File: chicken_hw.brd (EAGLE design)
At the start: 25.7 x 38.1 mm, 19 parts

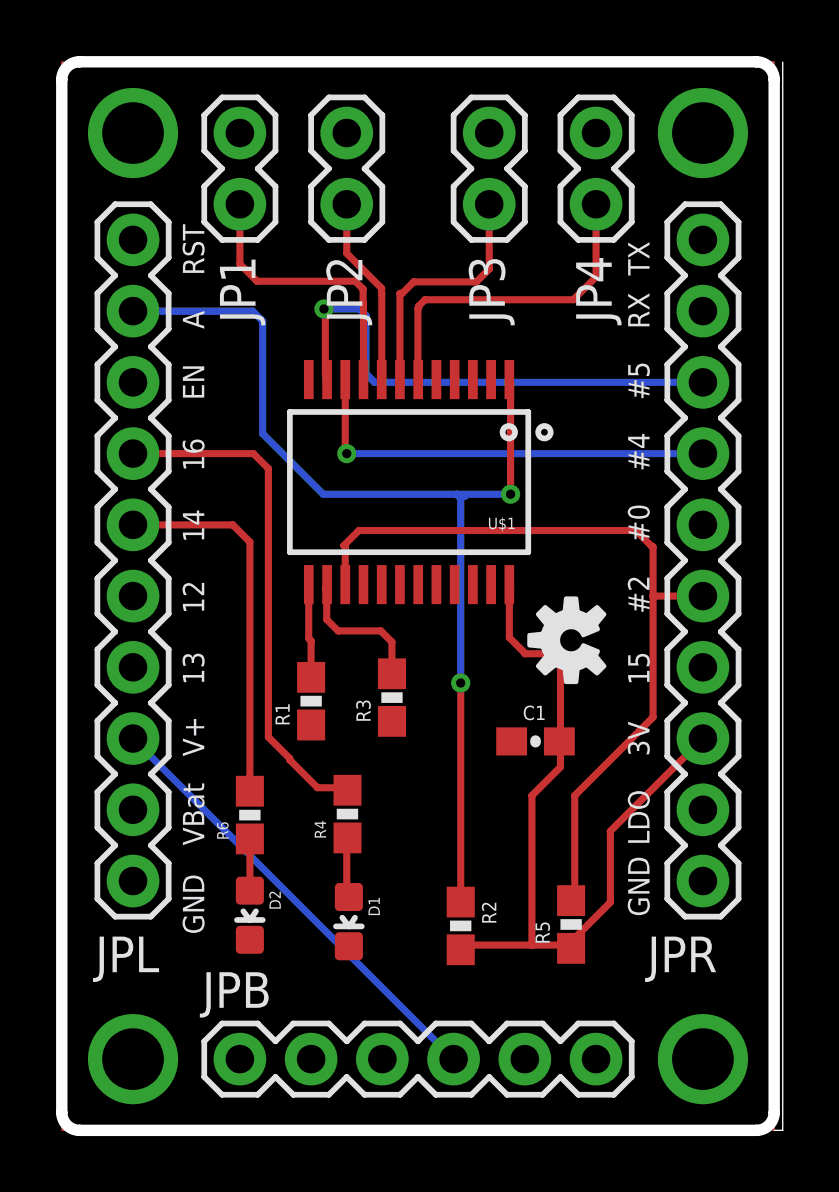
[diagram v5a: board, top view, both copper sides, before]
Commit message: Enable ESP8266 deepsleep by connecting GPIO16 to RESET - bump to ver 0.2
Remove led's on GPIO 16,14 and move them to GPIO 12, 13
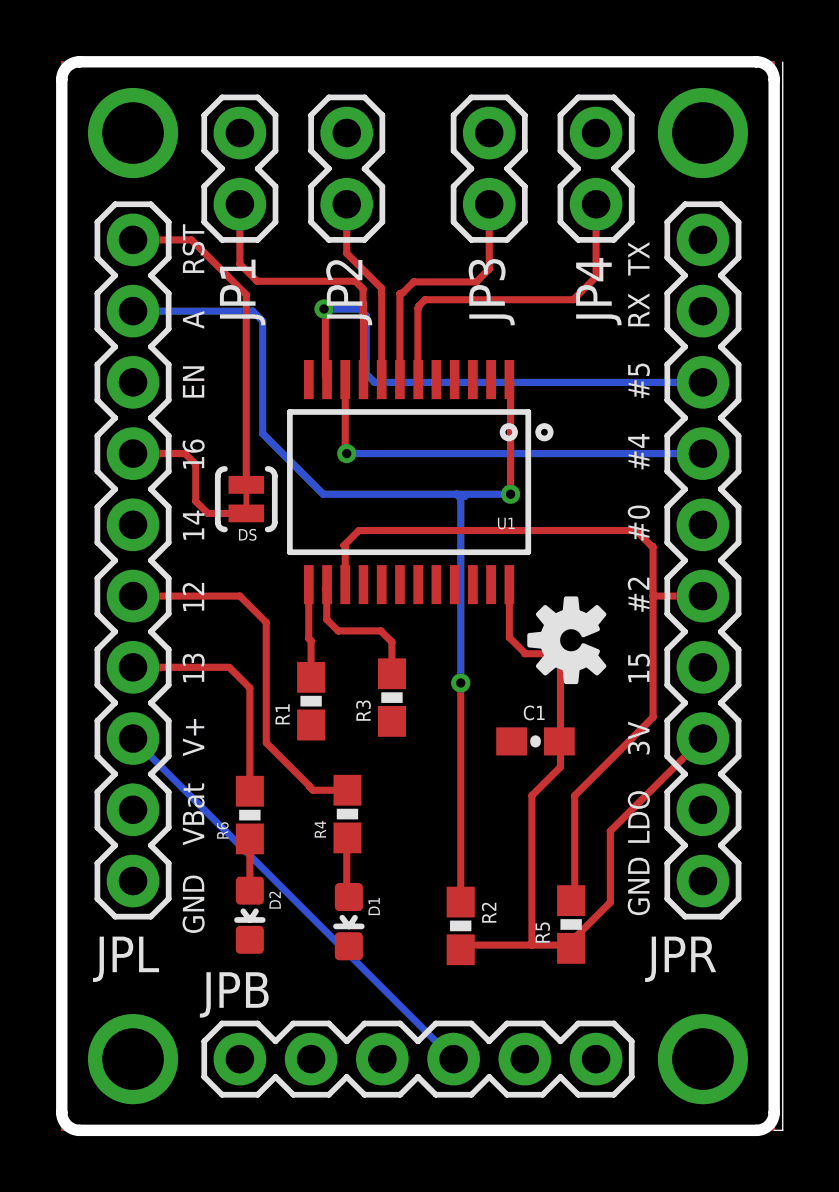
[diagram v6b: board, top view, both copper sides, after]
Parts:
- added DS: JUMPER-PAD-2-NC_BY_TRACE, SparkFun-Passives:PAD-JUMPER-2-NC_BY_TRACE_YES_SILK
- renumbered U$1 to U1
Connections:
- net GPIO12: now also R4.2
- net GPIO13: now also R6.2
- net GPIO14: no longer R6.2
- net GPIO16: now also DS.1; no longer R4.2
- net RST: now also DS.2
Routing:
- net GPIO14: track 13.3 -> 0.00 mm
- net GPIO12: track 0.00 -> 13.0 mm
- net GPIO16: track 18.3 -> 5.70 mm
- net RST: track 0.00 -> 11.6 mm
- net GPIO13: track 0.00 -> 8.15 mm
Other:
- board text added: "4-input Temp Sensor jason.k.holden@gmail.com ver 0.2 11-15-2015"
- board text removed: "4-input Temp Sensor jason.k.holden@gmail.com ver 0.1 11-8-2015"
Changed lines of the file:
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@@
 <text x="12.6492" y="19.1516" size="1.016" layer="22" font="vector" ratio="12" rot="MR90" align="center">4-input Temp Sensor
 jason.k.holden@gmail.com
-ver 0.1 11-8-2015</text>
+ver 0.2 11-15-2015</text>
 </plain>
 <attributes>
@@
 <attribute name="VALUE" x="19.685" y="33.02" size="1.27" layer="27" rot="R270"/>
 </element>
-<element name="U$1" library="SparkFun-AnalogIC" package="SSOP24" value="MUX-74HC4067SMD" x="12.3825" y="23.114" rot="R180">
+<element name="U1" library="SparkFun-AnalogIC" package="SSOP24" value="MUX-74HC4067SMD" x="12.3825" y="23.114" smashed="yes" rot="R180">
 <attribute name="PROD_ID" value="IC-08252" x="12.3825" y="23.114" size="1.778" layer="27" rot="R180" display="off"/>
+<attribute name="NAME" x="16.1925" y="21.844" size="0.4064" layer="25" font="vector" ratio="12" rot="R180"/>
+<attribute name="VALUE" x="15.1765" y="23.368" size="0.4064" layer="27" font="vector" ratio="12" rot="R180"/>
 </element>
 <element name="JP1" library="SparkFun-Connectors" package="1X02" value="" x="6.35" y="35.56" smashed="yes" rot="R270">
@@
 <element name="FRAME1" library="SparkFun-Aesthetics" package="CREATIVE_COMMONS" value="FRAME-LETTER" x="-3.937" y="-9.6012" smashed="yes"/>
 <element name="LOGO1" library="SparkFun-Aesthetics" package="OSHW-LOGO-S" value="OSHW-LOGOS" x="18.161" y="17.4752" rot="R90"/>
+<element name="DS" library="SparkFun-Passives" package="PAD-JUMPER-2-NC_BY_TRACE_YES_SILK" value="JUMPER-PAD-2-NC_BY_TRACE" x="6.5786" y="22.5044" smashed="yes" rot="R90">
+<attribute name="NAME" x="6.9723" y="21.4376" size="0.4064" layer="25" font="vector" ratio="12" rot="R180"/>
+</element>
 </elements>
 <signals>
 <signal name="RST">
 <contactref element="JPL" pad="1"/>
+<contactref element="DS" pad="2"/>
+<wire x1="6.5786" y1="23.0124" x2="6.5786" y2="29.7942" width="0.254" layer="1"/>
+<wire x1="6.5786" y1="29.7942" x2="4.6228" y2="31.75" width="0.254" layer="1"/>
+<wire x1="2.54" y1="31.75" x2="4.6228" y2="31.75" width="0.254" layer="1"/>
 </signal>
 <signal name="A">
 <contactref element="JPL" pad="2"/>
-<contactref element="U$1" pad="1"/>
+<contactref element="U1" pad="1"/>
 <contactref element="R2" pad="1"/>
 <via x="14.224" y="15.9512" extent="1-16" drill="0.3302"/>
@@
 <contactref element="JPL" pad="3"/>
 </signal>
-<signal name="GPIO16">
-<contactref element="JPL" pad="4"/>
-<contactref element="R4" pad="2"/>
-<wire x1="8.128" y1="13.208" x2="8.128" y2="13.2588" width="0.254" layer="1"/>
-<wire x1="8.128" y1="13.2588" x2="7.366" y2="14.0208" width="0.254" layer="1"/>
-<wire x1="7.366" y1="14.0208" x2="7.366" y2="23.5966" width="0.254" layer="1"/>
-<wire x1="2.54" y1="24.13" x2="6.8326" y2="24.13" width="0.254" layer="1"/>
-<wire x1="6.8326" y1="24.13" x2="7.366" y2="23.5966" width="0.254" layer="1"/>
-<wire x1="10.1854" y1="12.1276" x2="10.1854" y2="12.192" width="0.254" layer="1"/>
-<wire x1="10.1854" y1="12.192" x2="10.2108" y2="12.2174" width="0.254" layer="1"/>
-<wire x1="10.2108" y1="12.2174" x2="9.1186" y2="12.2174" width="0.254" layer="1"/>
-<wire x1="9.1186" y1="12.2174" x2="8.128" y2="13.208" width="0.254" layer="1"/>
-</signal>
-<signal name="GPIO14">
-<contactref element="JPL" pad="5"/>
-<contactref element="R6" pad="2"/>
-<wire x1="2.54" y1="21.59" x2="6.096" y2="21.59" width="0.254" layer="1"/>
-<wire x1="6.096" y1="21.59" x2="6.7056" y2="20.9804" width="0.254" layer="1"/>
-<wire x1="6.7056" y1="12.0895" x2="6.7056" y2="20.9804" width="0.254" layer="1"/>
-</signal>
 <signal name="GPIO12">
 <contactref element="JPL" pad="6"/>
+<contactref element="R4" pad="2"/>
+<wire x1="10.1854" y1="12.1276" x2="8.9544" y2="12.1276" width="0.254" layer="1"/>
+<wire x1="8.9544" y1="12.1276" x2="8.8392" y2="12.2428" width="0.254" layer="1"/>
+<wire x1="8.8392" y1="12.2428" x2="8.8392" y2="12.2682" width="0.254" layer="1"/>
+<wire x1="8.8392" y1="12.2682" x2="7.2898" y2="13.8176" width="0.254" layer="1"/>
+<wire x1="7.2898" y1="13.8176" x2="7.2898" y2="18.1102" width="0.254" layer="1"/>
+<wire x1="2.54" y1="19.05" x2="6.35" y2="19.05" width="0.254" layer="1"/>
+<wire x1="6.35" y1="19.05" x2="7.2898" y2="18.1102" width="0.254" layer="1"/>
 </signal>
 <signal name="GPIO13">
 <contactref element="JPL" pad="7"/>
+<contactref element="R6" pad="2"/>
+<wire x1="6.7056" y1="12.0895" x2="6.7056" y2="15.7734" width="0.254" layer="1"/>
+<wire x1="6.7056" y1="15.7734" x2="5.969" y2="16.51" width="0.254" layer="1"/>
+<wire x1="2.54" y1="16.51" x2="5.969" y2="16.51" width="0.254" layer="1"/>
 </signal>
 <signal name="VPLUS">
@@
 <signal name="GPIO4">
 <contactref element="JPR" pad="4"/>
-<contactref element="U$1" pad="10"/>
+<contactref element="U1" pad="10"/>
 <wire x1="22.86" y1="24.13" x2="10.16" y2="24.13" width="0.254" layer="16"/>
 <via x="10.16" y="24.13" extent="1-16" drill="0.3302"/>
@@
 <signal name="GPIO5">
 <contactref element="JPR" pad="3"/>
-<contactref element="U$1" pad="11"/>
+<contactref element="U1" pad="11"/>
 <wire x1="22.86" y1="26.67" x2="11.1506" y2="26.67" width="0.254" layer="16"/>
 <wire x1="9.398" y1="26.924" x2="9.4575" y2="26.77" width="0.254" layer="1"/>
@@
 <contactref element="JPB" pad="6"/>
 <contactref element="JPL" pad="10"/>
-<contactref element="U$1" pad="12"/>
+<contactref element="U1" pad="12"/>
 <contactref element="JP1" pad="1"/>
 <contactref element="JP2" pad="1"/>
@@
 <signal name="3.3V">
 <contactref element="JPR" pad="8"/>
-<contactref element="U$1" pad="24"/>
+<contactref element="U1" pad="24"/>
 <contactref element="C1" pad="1"/>
 <contactref element="R5" pad="2"/>
@@
 </signal>
 <signal name="EN_MUX">
-<contactref element="U$1" pad="15"/>
+<contactref element="U1" pad="15"/>
 <contactref element="JPR" pad="6"/>
 <contactref element="R5" pad="1"/>
@@
 <signal name="N$2">
 <contactref element="JP1" pad="2"/>
-<contactref element="U$1" pad="9"/>
+<contactref element="U1" pad="9"/>
 <wire x1="10.7575" y1="26.77" x2="10.7575" y2="29.4773" width="0.254" layer="1"/>
 <wire x1="10.4648" y1="30.2768" x2="6.9596" y2="30.2768" width="0.254" layer="1"/>
@@
 <signal name="N$3">
 <contactref element="JP2" pad="2"/>
-<contactref element="U$1" pad="8"/>
+<contactref element="U1" pad="8"/>
 <wire x1="11.4075" y1="26.77" x2="11.4075" y2="29.8167" width="0.254" layer="1"/>
 <wire x1="11.4075" y1="29.8167" x2="11.4046" y2="29.8196" width="0.254" layer="1"/>
@@
 <signal name="N$4">
 <contactref element="JP3" pad="2"/>
-<contactref element="U$1" pad="7"/>
+<contactref element="U1" pad="7"/>
 <wire x1="15.24" y1="33.02" x2="15.24" y2="30.7086" width="0.254" layer="1"/>
 <wire x1="15.24" y1="30.7086" x2="14.7828" y2="30.2514" width="0.254" layer="1"/>
@@
 <signal name="N$5">
 <contactref element="JP4" pad="2"/>
-<contactref element="U$1" pad="6"/>
+<contactref element="U1" pad="6"/>
 <wire x1="12.7" y1="26.924" x2="12.7" y2="29.3116" width="0.254" layer="1"/>
 <wire x1="12.7" y1="29.3116" x2="12.7254" y2="29.337" width="0.254" layer="1"/>
@@
 </signal>
 <signal name="N$1">
-<contactref element="U$1" pad="13"/>
+<contactref element="U1" pad="13"/>
 <contactref element="R1" pad="2"/>
 <wire x1="8.89" y1="16.1535" x2="8.89" y2="17.4498" width="0.254" layer="1"/>
@@
 </signal>
 <signal name="N$6">
-<contactref element="U$1" pad="14"/>
+<contactref element="U1" pad="14"/>
 <contactref element="R3" pad="2"/>
 <wire x1="9.398" y1="19.304" x2="9.4575" y2="19.458" width="0.254" layer="1"/>
@@
 <wire x1="6.7056" y1="10.3895" x2="6.7056" y2="8.5478" width="0.254" layer="1"/>
 </signal>
+<signal name="GPIO14">
+<contactref element="JPL" pad="5"/>
+</signal>
+<signal name="GPIO16">
+<contactref element="JPL" pad="4"/>
+<contactref element="DS" pad="1"/>
+<wire x1="2.54" y1="24.13" x2="4.3942" y2="24.13" width="0.254" layer="1"/>
+<wire x1="4.3942" y1="24.13" x2="4.7752" y2="23.749" width="0.254" layer="1"/>
+<wire x1="4.7752" y1="23.749" x2="4.7752" y2="22.4282" width="0.254" layer="1"/>
+<wire x1="4.7752" y1="22.4282" x2="5.207" y2="21.9964" width="0.254" layer="1"/>
+<wire x1="6.5786" y1="21.9964" x2="5.207" y2="21.9964" width="0.254" layer="1"/>
+</signal>
 </signals>

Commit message: Switch to 8to1 mux to save on cost
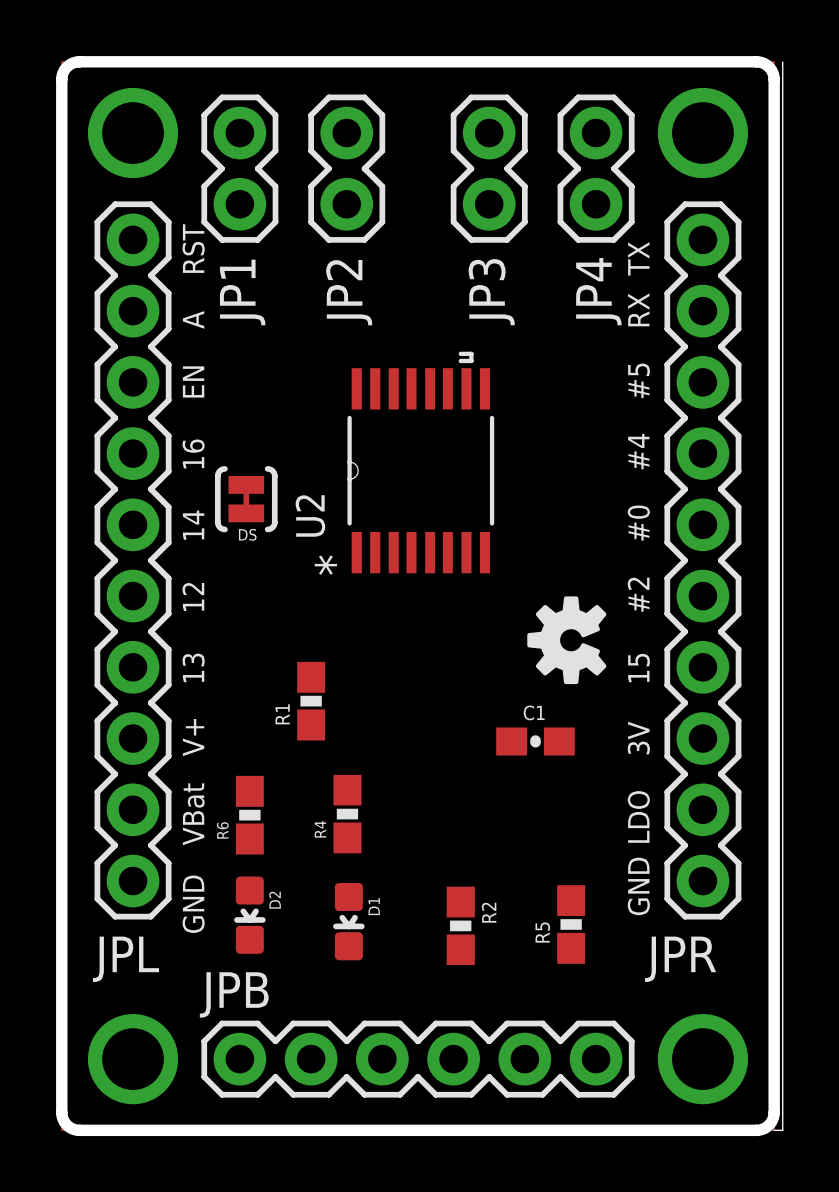
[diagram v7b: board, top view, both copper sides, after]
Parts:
- removed R3: 10k, SparkFun-Resistors:0603-RES
- removed U1: MUX-74HC4067SMD, SparkFun-AnalogIC:SSOP24
- added U2: CD74HC4051PWR, Texas Instruments_By_element14_Batch_1:SOP65P640X120-16N
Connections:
- removed net N$6: R3.2, U1.14
- new net VCC: U2.16
- net 3.3V: no longer U1.24
- net A: now also U2.3; no longer U1.1
- net EN_MUX: now also U2.6; no longer U1.15
- net GND: now also U2.7, U2.8; no longer R3.1, U1.12
- net GPIO4: now also U2.11; no longer U1.10
- net GPIO5: now also U2.10; no longer U1.11
- net N$1: no longer U1.13
- net N$2: now also U2.13; no longer U1.9
- net N$3: now also U2.14; no longer U1.8
- net N$4: now also U2.15; no longer U1.7
- net N$5: now also U2.12; no longer U1.6
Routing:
- net A: track 37.1 -> 0.00 mm, vias 2 -> 0
- net 3.3V: track 28.3 -> 0.00 mm
- net EN_MUX: track 28.3 -> 0.00 mm
- net GPIO5: track 18.4 -> 0.00 mm, vias 1 -> 0
- net VPLUS: track 16.2 -> 0.00 mm
- net GPIO4: track 15.4 -> 0.00 mm, vias 1 -> 0
- net GPIO12: track 13.0 -> 0.00 mm
- net N$5: track 11.8 -> 0.00 mm
- net RST: track 11.6 -> 0.00 mm
- net N$2: track 10.1 -> 0.00 mm
- net N$4: track 8.92 -> 0.00 mm
- net GPIO13: track 8.15 -> 0.00 mm
- net N$3: track 6.77 -> 0.00 mm
- net GPIO16: track 5.70 -> 0.00 mm
- net N$6: track 5.09 -> 0.00 mm
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
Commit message: Fully routed 8:1 mux, ready for production
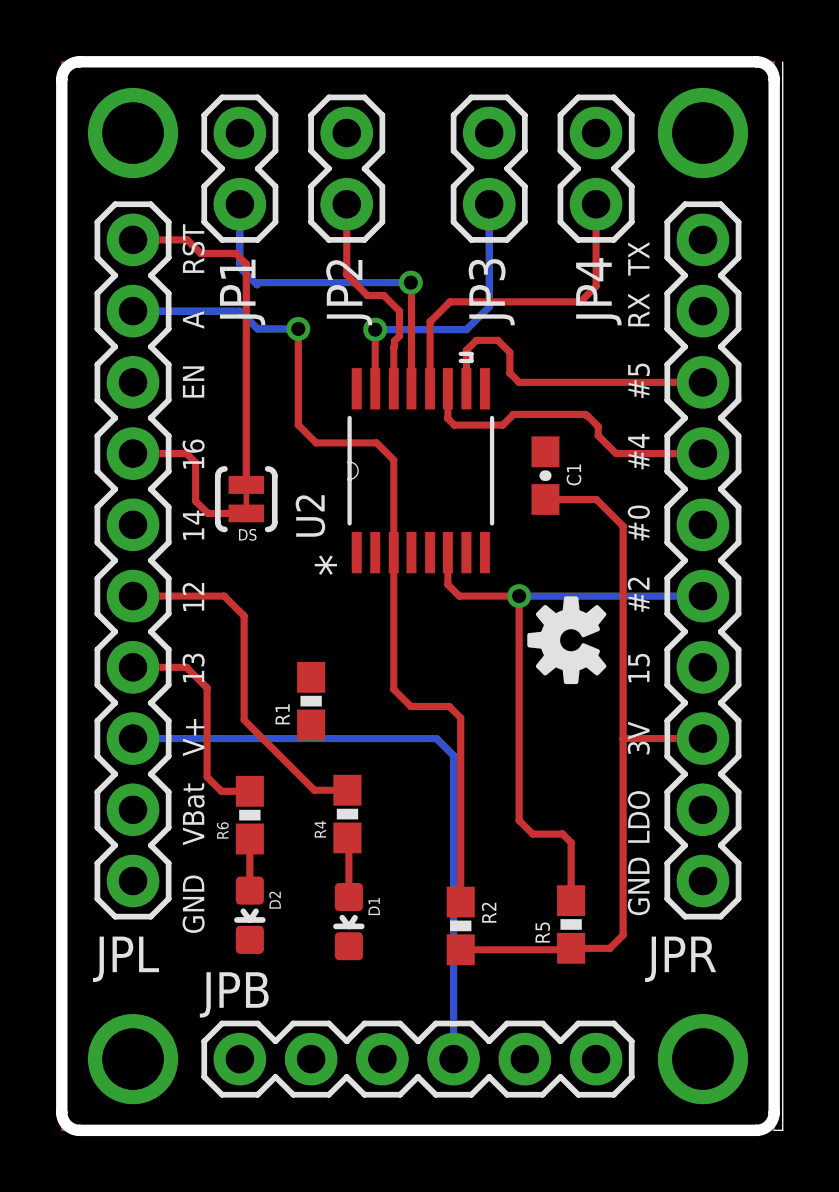
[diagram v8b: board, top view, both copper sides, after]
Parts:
- moved C1 9.48 mm to (17.2, 23.3), turned to 90 degrees
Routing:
- net A: track 0.00 -> 31.1 mm, vias 0 -> 1
- net 3.3V: track 0.00 -> 26.6 mm
- net EN_MUX: track 0.00 -> 22.7 mm, vias 0 -> 1
- net VPLUS: track 0.00 -> 22.5 mm
- net GPIO12: track 0.00 -> 12.7 mm
- net N$2: track 0.00 -> 12.4 mm, vias 0 -> 1
- net RST: track 0.00 -> 12.3 mm
- net N$5: track 0.00 -> 11.8 mm
- net GPIO4: track 0.00 -> 11.2 mm
- net GPIO5: track 0.00 -> 11.0 mm
- net N$4: track 0.00 -> 10.2 mm, vias 0 -> 1
- net GPIO13: track 0.00 -> 7.86 mm
- net N$3: track 0.00 -> 7.78 mm
- net GPIO16: track 0.00 -> 5.73 mm
- net N$8: track 0.00 -> 2.13 mm
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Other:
- board text added: "4-input Temp Sensor jason.k.holden@gmail.com ver 0.3 12-13-2015"
- board text removed: "4-input Temp Sensor jason.k.holden@gmail.com ver 0.2 11-15-2015"
